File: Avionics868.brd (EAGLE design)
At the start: 88.8 x 22.9 mm, 61 parts, among them SW1 SPST_TACT-KMR2, U1 ATSAMD21G18_QFN, U2 SPX3819M5-L-3-0, U3 MCP73831T-2ACI/OT, U4 MPU-9250, U5 SIM868, U6 BMP180, X1 JSTPH, X2 32.768, X3 microUSB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

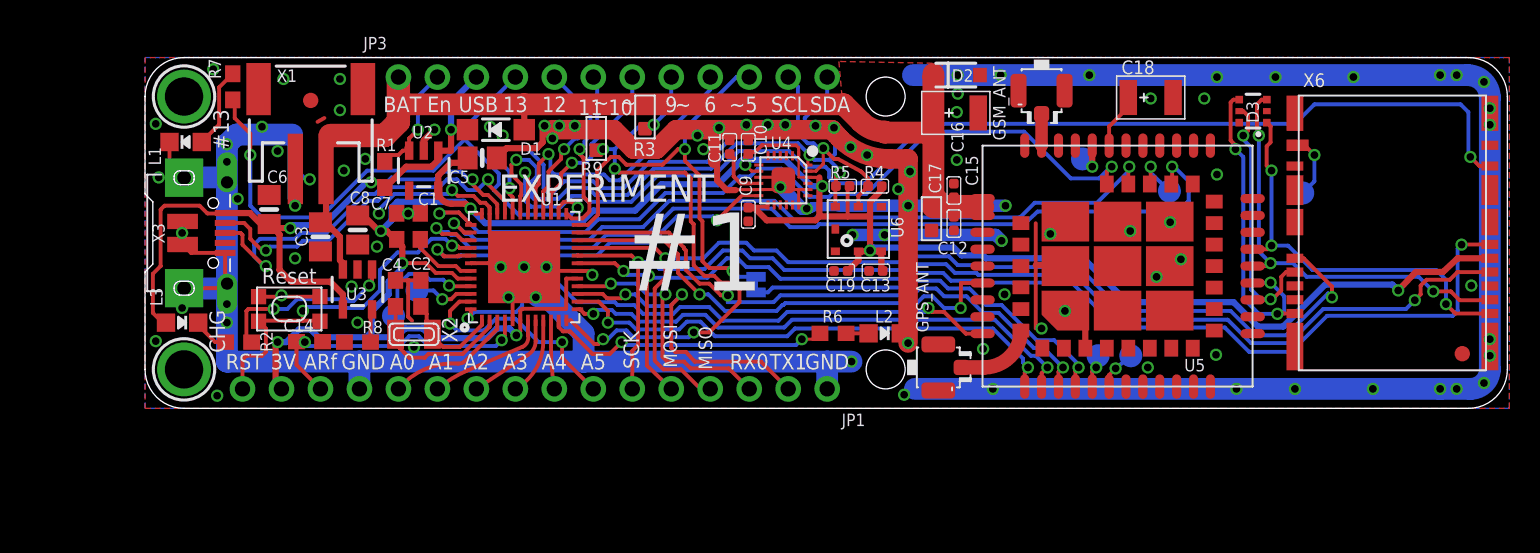
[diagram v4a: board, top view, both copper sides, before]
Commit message: Added bypass capacitors ++
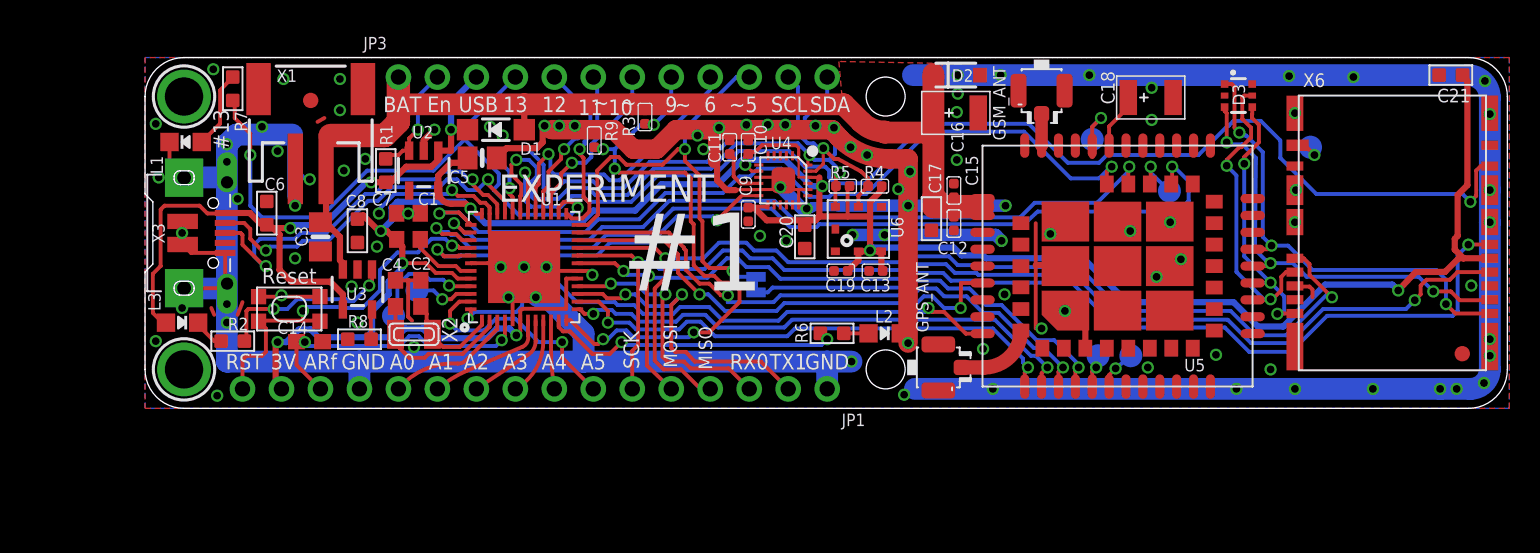
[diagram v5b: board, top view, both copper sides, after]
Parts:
- added C20, C21: 10uf, Seeed-Capacitor-2016:C0603
- C3: value 10µF -> 10uF
- C6, C8: value 10µF -> 10uf; device microbuilder:0805-NO -> Seeed-Capacitor-2016:C0603
- R1: value 100k -> 100K 1/10W; device microbuilder:0603-NO -> Seeed-Resistor-2016:R0603
- R2, R6: value 1K -> 1K 1/10W; device microbuilder:0603-NO -> Seeed-Resistor-2016:R0603
- R3, R9: value 100K 1/10W -> 100K; device Seeed-Resistor-2016:R0603 -> Seeed-Resistor-2016:R0402
- R7: value 2.2K -> 1K 1/10W; device microbuilder:0603-NO -> Seeed-Resistor-2016:R0603
- R8: value 10K\ -> 10K 1/10W; device microbuilder:0603-NO -> Seeed-Resistor-2016:R0603
- moved TP3 3.03 mm to (75.9, 17.0)
- moved TP5 1.42 mm to (61.7, 17.5)
- moved D3 1.39 mm to (71.2, 20.4), turned to 270 degrees
- moved R2 0.39 mm to (5.71, 4.38), turned to 90 degrees
- moved C6 0.28 mm to (7.93, 12.7), turned to 180 degrees
- moved R1 0.26 mm to (15.7, 15.5), turned to 180 degrees
- moved R8 0.23 mm to (14.0, 4.51), turned to 270 degrees
- moved R9 0.18 mm to (29.3, 17.5)
- moved R7 0.13 mm to (5.71, 20.8), turned to 180 degrees
- moved R6 0.06 mm to (44.8, 4.89), turned to 90 degrees
- moved C8 0.06 mm to (13.8, 11.6), turned to 0 degrees
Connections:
- net +3V: now also C20.1, C21.1
- net GND: now also C20.2, C21.2
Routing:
- net +3V: track 161.5 -> 174.7 mm
- net SIM_VDD: track 26.7 -> 30.5 mm
- net SIM_CLK: track 21.5 -> 17.8 mm
- net GND: track 314.8 -> 317.9 mm, vias 103 -> 105
- net D7/SD_CS: track 76.0 -> 79.1 mm
- net SIM_DATA: track 18.0 -> 20.3 mm
- net SD_DET: track 4.15 -> 1.95 mm
- net RF_SYNC: track 2.22 -> 4.34 mm
- net D8/GLED: track 18.9 -> 19.8 mm
- net SIM_RST: track 28.0 -> 28.6 mm
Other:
- board text removed: "CHG"

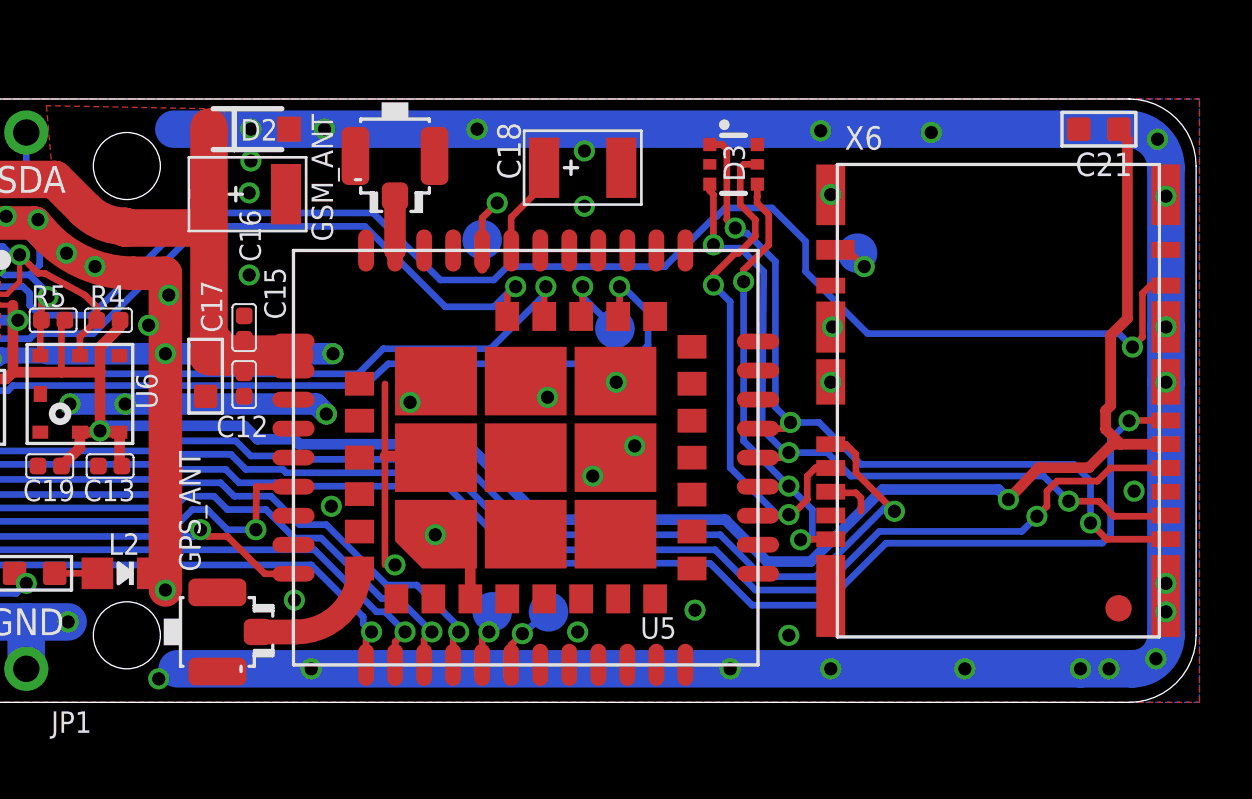
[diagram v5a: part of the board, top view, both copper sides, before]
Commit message: More bypass for SIM and SD
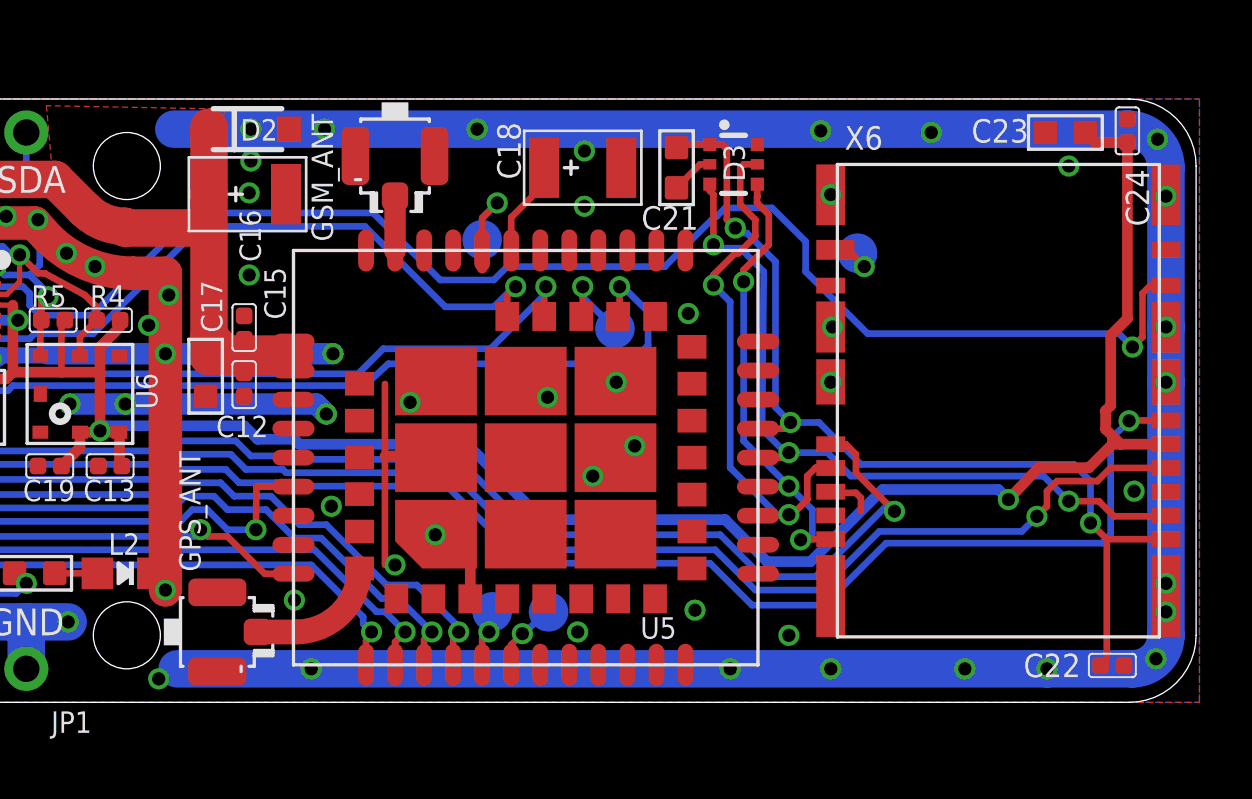
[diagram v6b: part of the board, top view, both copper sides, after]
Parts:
- removed U$35: FIDUCIAL"", microbuilder:FIDUCIAL_1MM
- added C22, C24: 100nf, Seeed-Capacitor-2016:C0402
- added C23: 10uf, Seeed-Capacitor-2016:C0603
- moved C21 16.1 mm to (69.1, 20.3), turned to 0 degrees
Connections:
- net +3V: now also C23.1, C24.2; no longer C21.1
- net GND: now also C22.1, C23.2, C24.1
- net SIM_VDD: now also C21.1, C22.2
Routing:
- net SIM_VDD: track 30.5 -> 36.7 mm
- net GND: track 317.9 -> 319.6 mm, vias 105 -> 106
- net +3V: track 174.7 -> 175.8 mm
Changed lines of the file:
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@@
 <attribute name="BOM" value="EXCLUDE" x="10.795" y="20.066" size="1.778" layer="27" rot="R270" display="off"/>
-</element>
-<element name="U$35" library="microbuilder" package="FIDUCIAL_1MM" value="FIDUCIAL&quot;&quot;" x="85.8357" y="3.563" smashed="yes" rot="R270">
-<attribute name="BOM" value="EXCLUDE" x="85.8357" y="3.563" size="1.778" layer="27" rot="R270" display="off"/>
 </element>
 <element name="SW1" library="adafruit" package="KMR2" value="SPST_TACT-KMR2" x="9.398" y="6.477" smashed="yes" rot="R180"/>
@@
 <attribute name="NAME" x="42.7355" y="12.446" size="0.635" layer="33" ratio="10" rot="R270"/>
 </element>
-<element name="C21" library="Seeed-Capacitor-2016" package="C0603" value="10uf" x="85.09" y="21.717" rot="R270">
-<attribute name="VALUE" value="10uf" x="85.09" y="21.717" size="1.778" layer="27" rot="R270" display="off"/>
-<attribute name="MPN" value="CC0603KRX5R6BB106" x="85.09" y="21.717" size="1.778" layer="27" rot="R270" display="off"/>
+<element name="C21" library="Seeed-Capacitor-2016" package="C0603" value="10uf" x="69.088" y="20.2565" smashed="yes">
+<attribute name="VALUE" value="10uf" x="69.088" y="20.2565" size="1.778" layer="27" display="off"/>
+<attribute name="MPN" value="CC0603KRX5R6BB106" x="69.088" y="20.2565" size="1.778" layer="27" display="off"/>
+<attribute name="NAME" x="67.7545" y="17.907" size="0.889" layer="25" ratio="11"/>
+<attribute name="VALUE" x="67.5005" y="21.5265" size="0.635" layer="27" ratio="10" rot="R270"/>
+<attribute name="NAME" x="68.834" y="21.5265" size="0.635" layer="33" ratio="10" rot="R270"/>
+</element>
+<element name="C22" library="Seeed-Capacitor-2016" package="C0402" value="100nf" x="85.598" y="1.397" smashed="yes" rot="R270">
+<attribute name="MPN" value="CC0402KRX7R8BB104" x="85.598" y="1.397" size="1.778" layer="27" rot="R270" display="off"/>
+<attribute name="NAME" x="82.2325" y="0.9525" size="0.889" layer="25" ratio="11"/>
+<attribute name="VALUE" x="86.995" y="2.921" size="0.635" layer="27" font="vector" ratio="10" rot="R180"/>
+</element>
+<element name="C23" library="Seeed-Capacitor-2016" package="C0603" value="10uf" x="83.82" y="21.59" smashed="yes" rot="R270">
+<attribute name="MPN" value="CC0603KRX5R6BB106" x="93.98" y="26.67" size="1.778" layer="27" rot="R270" display="off"/>
+<attribute name="NAME" x="82.423" y="22.098" size="0.889" layer="25" ratio="11" rot="R180"/>
+<attribute name="VALUE" x="85.09" y="23.1775" size="0.635" layer="27" ratio="10" rot="R180"/>
+<attribute name="NAME" x="85.09" y="21.844" size="0.635" layer="33" ratio="10" rot="R180"/>
+</element>
+<element name="C24" library="Seeed-Capacitor-2016" package="C0402" value="100nf" x="86.1695" y="21.6535" smashed="yes">
+<attribute name="MPN" value="CC0402KRX7R8BB104" x="76.0095" y="28.0035" size="1.778" layer="27" display="off"/>
+<attribute name="NAME" x="86.995" y="18.034" size="0.889" layer="25" ratio="11" rot="R90"/>
+<attribute name="VALUE" x="84.6455" y="23.0505" size="0.635" layer="27" font="vector" ratio="10" rot="R270"/>
 </element>
 </elements>
@@
 <wire x1="87.63" y1="12.1285" x2="87.63" y2="2.54" width="1.4224" layer="16"/>
 <wire x1="87.63" y1="2.54" x2="86.36" y2="1.27" width="1.4224" layer="16" curve="-90"/>
-<wire x1="86.36" y1="1.27" x2="84.3915" y2="1.27" width="1.4224" layer="16"/>
-<wire x1="84.3915" y1="1.27" x2="50.165" y2="1.27" width="1.4224" layer="16"/>
+<wire x1="86.36" y1="1.27" x2="83.1215" y2="1.27" width="1.4224" layer="16"/>
+<wire x1="83.1215" y1="1.27" x2="50.165" y2="1.27" width="1.4224" layer="16"/>
 <wire x1="34.6075" y1="18.161" x2="37.2745" y2="18.161" width="1.27" layer="1"/>
 <via x="5.334" y="17.2085" extent="1-16" drill="0.5"/>
@@
 <via x="46.0375" y="3.048" extent="1-16" drill="0.5"/>
 <via x="55.245" y="1.27" extent="1-16" drill="0.5"/>
-<via x="85.471" y="1.27" extent="1-16" drill="0.5"/>
 <via x="23.6855" y="7.239" extent="1-16" drill="0.5"/>
 <via x="25.4635" y="7.239" extent="1-16" drill="0.5"/>
@@
 <wire x1="28.5115" y1="8.9535" x2="28.956" y2="8.9535" width="0.254" layer="1"/>
 <via x="65.3415" y="2.667" extent="1-16" drill="0.5"/>
-<via x="84.3915" y="1.27" extent="1-16" drill="0.5"/>
+<via x="83.1215" y="1.27" extent="1-16" drill="0.5"/>
 <via x="87.63" y="3.429" extent="1-16" drill="0.5"/>
 <via x="87.63" y="4.5085" extent="1-16" drill="0.5"/>
@@
 <via x="41.783" y="10.922" extent="1-16" drill="0.5"/>
 <via x="73.3425" y="2.54" extent="1-16" drill="0.5"/>
+<contactref element="C22" pad="1"/>
+<via x="69.5325" y="14.732" extent="1-16" drill="0.5"/>
+<wire x1="70.347" y1="20.3835" x2="69.977" y2="20.3835" width="0.254" layer="1"/>
+<wire x1="69.977" y1="20.3835" x2="69.088" y2="19.4945" width="0.254" layer="1"/>
+<contactref element="C24" pad="1"/>
+<contactref element="C23" pad="2"/>
+<via x="83.947" y="20.32" extent="1-16" drill="0.5"/>
 <wire x1="2.545" y1="15.03" x2="2.54" y2="15.0495" width="0" layer="19" extent="16-16"/>
 <wire x1="2.54" y1="7.8105" x2="2.545" y2="7.83" width="0" layer="19" extent="16-16"/>
@@
 <wire x1="82.804" y1="8.89" x2="84.709" y2="8.89" width="0.4064" layer="1"/>
 <contactref element="C20" pad="1"/>
-<contactref element="C21" pad="1"/>
 <wire x1="85.344" y1="11.049" x2="85.5345" y2="11.2395" width="0.4064" layer="1"/>
 <wire x1="85.5345" y1="11.2395" x2="85.5345" y2="13.9065" width="0.4064" layer="1"/>
 <wire x1="85.5345" y1="13.9065" x2="86.1695" y2="14.5415" width="0.4064" layer="1"/>
-<wire x1="86.1695" y1="14.5415" x2="86.1695" y2="21.336" width="0.4064" layer="1"/>
+<wire x1="86.1695" y1="14.5415" x2="86.1695" y2="21.209" width="0.4064" layer="1"/>
 <wire x1="85.344" y1="11.049" x2="85.344" y2="10.3505" width="0.4064" layer="1"/>
 <wire x1="85.344" y1="10.3505" x2="85.9145" y2="9.78" width="0.4064" layer="1"/>
@@
 <wire x1="84.709" y1="8.89" x2="85.599" y2="9.78" width="0.4064" layer="1"/>
 <wire x1="85.599" y1="9.78" x2="85.9145" y2="9.78" width="0.4064" layer="1"/>
-<wire x1="86.1695" y1="21.336" x2="85.852" y2="21.6535" width="0.4064" layer="1"/>
-<wire x1="85.852" y1="21.6535" x2="85.852" y2="21.717" width="0.4064" layer="1"/>
 <wire x1="42.9895" y1="11.938" x2="43.18" y2="12.1285" width="0.4064" layer="1"/>
 <wire x1="43.18" y1="12.1285" x2="43.18" y2="12.2555" width="0.4064" layer="1"/>
+<contactref element="C23" pad="1"/>
+<contactref element="C24" pad="2"/>
+<wire x1="86.1695" y1="21.209" x2="84.963" y2="21.209" width="0.4064" layer="1"/>
+<wire x1="84.963" y1="21.209" x2="84.582" y2="21.59" width="0.4064" layer="1"/>
 </signal>
 <signal name="VBUS">
@@
 <wire x1="71.755" y1="17.78" x2="71.501" y2="17.78" width="0.254" layer="16"/>
 <wire x1="71.501" y1="17.78" x2="71.3105" y2="17.9705" width="0.254" layer="16"/>
+<contactref element="C22" pad="2"/>
+<wire x1="85.387" y1="6.18" x2="85.387" y2="1.6305" width="0.254" layer="1"/>
+<wire x1="85.387" y1="1.6305" x2="85.1535" y2="1.397" width="0.254" layer="1"/>
+<contactref element="C21" pad="1"/>
+<wire x1="70.347" y1="21.1335" x2="69.203" y2="21.1335" width="0.254" layer="1"/>
+<wire x1="69.203" y1="21.1335" x2="69.088" y2="21.0185" width="0.254" layer="1"/>
 </signal>
 <signal name="SIM_DATA">

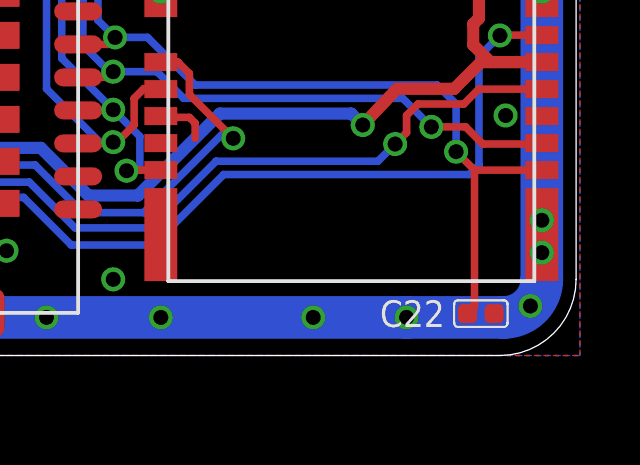
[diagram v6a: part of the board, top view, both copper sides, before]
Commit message: Removed bRestrict pads from SD/SIM connector
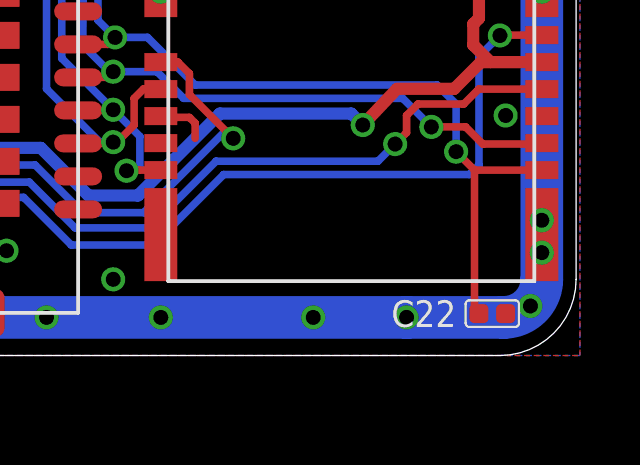
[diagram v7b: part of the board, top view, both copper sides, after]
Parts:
- moved C22 0.38 mm to (86.0, 1.40)
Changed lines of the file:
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@@
 <attribute name="NAME" x="68.834" y="21.5265" size="0.635" layer="33" ratio="10" rot="R270"/>
 </element>
-<element name="C22" library="Seeed-Capacitor-2016" package="C0402" value="100nf" x="85.598" y="1.397" smashed="yes" rot="R270">
-<attribute name="MPN" value="CC0402KRX7R8BB104" x="85.598" y="1.397" size="1.778" layer="27" rot="R270" display="off"/>
-<attribute name="NAME" x="82.2325" y="0.9525" size="0.889" layer="25" ratio="11"/>
-<attribute name="VALUE" x="86.995" y="2.921" size="0.635" layer="27" font="vector" ratio="10" rot="R180"/>
+<element name="C22" library="Seeed-Capacitor-2016" package="C0402" value="100nf" x="85.979" y="1.397" smashed="yes" rot="R270">
+<attribute name="MPN" value="CC0402KRX7R8BB104" x="85.979" y="1.397" size="1.778" layer="27" rot="R270" display="off"/>
+<attribute name="NAME" x="82.6135" y="0.9525" size="0.889" layer="25" ratio="11"/>
+<attribute name="VALUE" x="87.376" y="2.921" size="0.635" layer="27" font="vector" ratio="10" rot="R180"/>
 </element>
 <element name="C23" library="Seeed-Capacitor-2016" package="C0603" value="10uf" x="83.82" y="21.59" smashed="yes" rot="R270">
@@
 <contactref element="C22" pad="2"/>
 <wire x1="85.387" y1="6.18" x2="85.387" y2="1.6305" width="0.254" layer="1"/>
-<wire x1="85.387" y1="1.6305" x2="85.1535" y2="1.397" width="0.254" layer="1"/>
+<wire x1="85.387" y1="1.6305" x2="85.5345" y2="1.397" width="0.254" layer="1"/>
 <contactref element="C21" pad="1"/>
 <wire x1="70.347" y1="21.1335" x2="69.203" y2="21.1335" width="0.254" layer="1"/>
